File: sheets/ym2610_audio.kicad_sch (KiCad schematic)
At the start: 56 parts, among them J3 SMK S-G8043, Q101 2SC1815, Q102 2SC1815, U26 YM3016D, U27 YM2610, U28 PC4741, U29 PC4741

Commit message: Schematics Footprint updates
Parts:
- U26: footprint Package_DIP:DIP-16_W7.62mm -> 1_NeoGeoLibrary:DIP-16_W7.62mm
- U28, U29: footprint Package_DIP:DIP-14_W7.62mm -> 1_NeoGeoLibrary:DIP-14_W7.62mm
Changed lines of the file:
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@@
       (effects (font (size 1.27 1.27)))
     )
-    (property "Footprint" "Package_DIP:DIP-14_W7.62mm" (at 322.072 53.721 0)
+    (property "Footprint" "1_NeoGeoLibrary:DIP-14_W7.62mm" (at 322.072 53.721 0)
       (effects (font (size 1.27 1.27)) hide)
     )
@@
       (effects (font (size 1.27 1.27)))
     )
-    (property "Footprint" "Package_DIP:DIP-14_W7.62mm" (at 207.264 51.181 0)
+    (property "Footprint" "1_NeoGeoLibrary:DIP-14_W7.62mm" (at 207.264 51.181 0)
       (effects (font (size 1.27 1.27)) hide)
     )
@@
       (effects (font (size 1.27 1.27)))
     )
-    (property "Footprint" "Package_DIP:DIP-14_W7.62mm" (at 239.776 84.201 0)
+    (property "Footprint" "1_NeoGeoLibrary:DIP-14_W7.62mm" (at 239.776 84.201 0)
       (effects (font (size 1.27 1.27)) hide)
     )
@@
       (effects (font (size 1.27 1.27)))
     )
-    (property "Footprint" "Package_DIP:DIP-14_W7.62mm" (at 149.479 210.693 0)
+    (property "Footprint" "1_NeoGeoLibrary:DIP-14_W7.62mm" (at 149.479 210.693 0)
       (effects (font (size 1.27 1.27)) hide)
     )
@@
       (effects (font (size 1.27 1.27)))
     )
-    (property "Footprint" "Package_DIP:DIP-14_W7.62mm" (at 239.776 119.761 0)
+    (property "Footprint" "1_NeoGeoLibrary:DIP-14_W7.62mm" (at 239.776 119.761 0)
       (effects (font (size 1.27 1.27)) hide)
     )
@@
       (effects (font (size 1.27 1.27)))
     )
-    (property "Footprint" "Package_DIP:DIP-16_W7.62mm" (at 179.324 132.461 0)
+    (property "Footprint" "1_NeoGeoLibrary:DIP-16_W7.62mm" (at 179.324 132.461 0)
       (effects (font (size 1.27 1.27)) hide)
     )
@@
       (effects (font (size 1.27 1.27)))
     )
-    (property "Footprint" "Package_DIP:DIP-14_W7.62mm" (at 322.072 81.661 0)
+    (property "Footprint" "1_NeoGeoLibrary:DIP-14_W7.62mm" (at 322.072 81.661 0)
       (effects (font (size 1.27 1.27)) hide)
     )
@@
       (effects (font (size 1.27 1.27)))
     )
-    (property "Footprint" "Package_DIP:DIP-14_W7.62mm" (at 149.479 224.663 0)
+    (property "Footprint" "1_NeoGeoLibrary:DIP-14_W7.62mm" (at 149.479 224.663 0)
       (effects (font (size 1.27 1.27)) hide)
     )
@@
       (effects (font (size 1.27 1.27)))
     )
-    (property "Footprint" "Package_DIP:DIP-14_W7.62mm" (at 239.776 155.321 0)
-      (effects (font (size 1.27 1.27)) hide)
-    )
+    (property "Footprint" "1_NeoGeoLibrary:DIP-14_W7.62mm" (at 239.776 155.321 0)
+      (effects (font (size 1.27 1.27)) hide)
+    )

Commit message: Final update to Schematics Footprints Silkscreens
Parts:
- C13, C14: value 0.0022uF -> 272M
- C22, C23: value 10uF -> 1nF
- R39, R40, R41, R42: value 4.7KΩ -> 1KΩ
- RV1: value Headphone Slider -> Headphone Slider (0-1K)
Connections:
- net GND: no longer RV1.3
- no-connect marks 0 -> 1
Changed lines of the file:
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@@
   (junction (at 169.164 109.601) (diameter 0) (color 0 0 0 0)
   )
-  (junction (at 58.928 217.551) (diameter 0) (color 0 0 0 0)
-  )
   (junction (at 114.3 217.678) (diameter 0) (color 0 0 0 0)
   )
@@
   (junction (at 119.761 224.663) (diameter 0) (color 0 0 0 0)
   )
+  (no_connect (at 58.928 220.218))
   (bus_entry (at 140.97 53.721) (size -2.54 2.54)
     (stroke (width 0) (type default))
@@
     (stroke (width 0) (type default))
   )
-  (wire (pts (xy 58.928 217.551) (xy 58.928 220.218))
-    (stroke (width 0) (type default))
-  )
   (wire (pts (xy 225.425 208.788) (xy 225.425 213.233))
     (stroke (width 0) (type default))
@@
       (effects (font (size 1.27 1.27)))
     )
-    (property "Value" "0.0022uF" (at 200.152 147.574 90)
+    (property "Value" "272M" (at 200.152 147.574 90)
       (effects (font (size 1.27 1.27)))
     )
@@
       (effects (font (size 1.27 1.27)) (justify right))
     )
-    (property "Value" "Headphone Slider" (at 54.991 212.09 90)
+    (property "Value" "Headphone Slider (0-1K)" (at 54.991 212.09 90)
       (effects (font (size 1.27 1.27)) (justify right))
     )
@@
       (effects (font (size 1.27 1.27)))
     )
-    (property "Value" "4.7KΩ" (at 271.018 60.96 90)
+    (property "Value" "1KΩ" (at 271.018 60.96 90)
       (effects (font (size 1.27 1.27)))
     )
@@
       (effects (font (size 1.27 1.27)))
     )
-    (property "Value" "4.7KΩ" (at 271.018 79.502 90)
+    (property "Value" "1KΩ" (at 271.018 79.502 90)
       (effects (font (size 1.27 1.27)))
     )
@@
       (effects (font (size 1.27 1.27)))
     )
-    (property "Value" "4.7KΩ" (at 287.782 79.502 90)
+    (property "Value" "1KΩ" (at 287.782 79.502 90)
       (effects (font (size 1.27 1.27)))
     )
@@
       (effects (font (size 1.27 1.27)))
     )
-    (property "Value" "4.7KΩ" (at 287.782 60.96 90)
+    (property "Value" "1KΩ" (at 287.782 60.96 90)
       (effects (font (size 1.27 1.27)))
     )
@@
   (symbol (lib_id "Device:C_Small") (at 58.928 249.555 0) (unit 1)
     (in_bom yes) (on_board yes) (dnp no) (fields_autoplaced)
-    (property "Reference" "C22" (at 61.595 248.2912 0)
+    (property "Reference" "C22" (at 62.23 248.9263 0)
       (effects (font (size 1.27 1.27)) (justify left))
     )
-    (property "Value" "10uF" (at 61.595 250.8312 0)
+    (property "Value" "1nF" (at 62.23 251.4663 0)
       (effects (font (size 1.27 1.27)) (justify left))
     )
@@
       (effects (font (size 1.27 1.27)) (justify left))
     )
-    (property "Value" "0.0022uF" (at 224.282 117.221 0)
+    (property "Value" "272M" (at 224.282 117.221 0)
       (effects (font (size 1.27 1.27)) (justify left))
     )
@@
       (effects (font (size 1.27 1.27)))
     )
-    (property "Value" "10uF" (at 62.865 186.817 0)
+    (property "Value" "1nF" (at 62.865 186.817 0)
       (effects (font (size 1.27 1.27)))
     )

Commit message: Some tweaks
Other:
- company: (none) -> SNK
- title: (none) -> NeoGeo AES
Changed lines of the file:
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@@
 (kicad_sch (version 20230121) (generator eeschema)
   (paper "A3")
+  (title_block
+    (title "NeoGeo AES")
+    (date "2023-08-19")
+    (rev "3.5")
+    (company "SNK")
+    (comment 3 "https://github.com/Board-Folk")
+    (comment 4 "Recreated By The Board Folk Team")
+  )
   (junction (at 128.905 135.001) (diameter 0) (color 0 0 0 0)
   )

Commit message: Updates to PCB Move P2 Joystick Port Move Memory Card Move Holes at top right Silkscreen added Update Titles
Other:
- title: NeoGeo AES -> NeoGeo AES 3-5
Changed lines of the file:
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@@
   (paper "A3")
   (title_block
-    (title "NeoGeo AES")
-    (date "2023-08-19")
-    (rev "3.5")
+    (title "NeoGeo AES 3-5")
+    (date "2023-08-27")
+    (rev "BF1.1")
     (company "SNK")
     (comment 3 "https://github.com/Board-Folk")

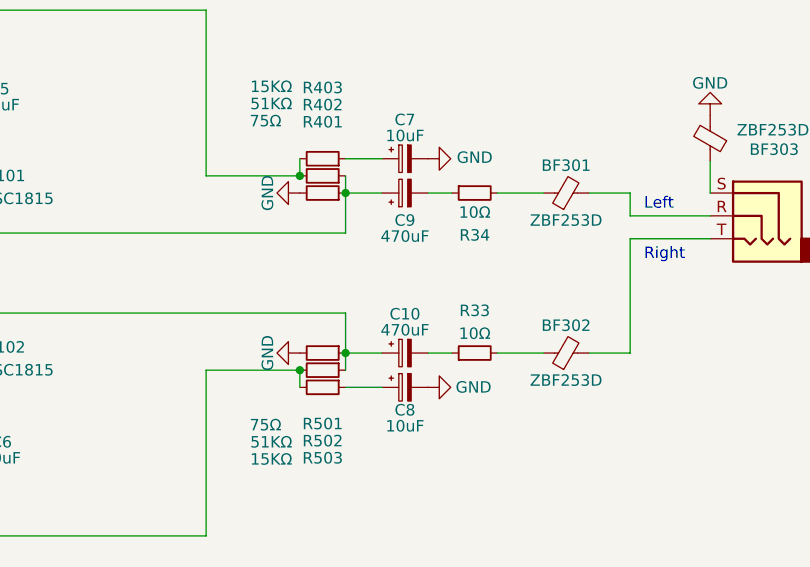
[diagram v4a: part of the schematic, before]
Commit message: Adding Mouser Part Numbers
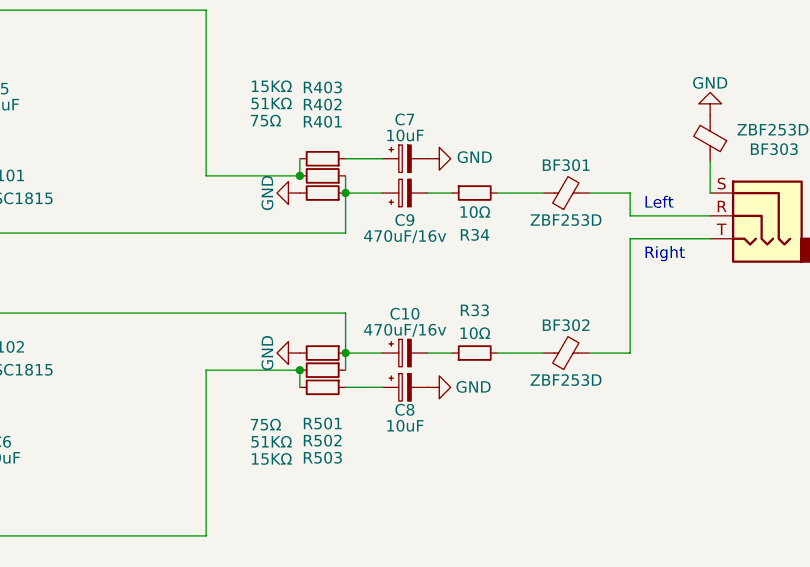
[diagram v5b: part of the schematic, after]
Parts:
- BF301, BF302, BF303: Mouser (none) -> 80-B-06-R-25
- C10, C9: value 470uF -> 470uF/16v; Mouser (none) -> 647-UHE1C471MPD6
- C11, C12, C2, C20, C24, C25, C301, C4, C5, C6, C7, C8: Mouser (none) -> 667-ECA-1CM100I
- C13, C14: Mouser (none) -> 80-MMK5272K63J01TA18
- C22, C23: Mouser (none) -> 810-FG28C0G1H102JNT6
- C3: Mouser (none) -> 810-FG28C0G2A680JNT6

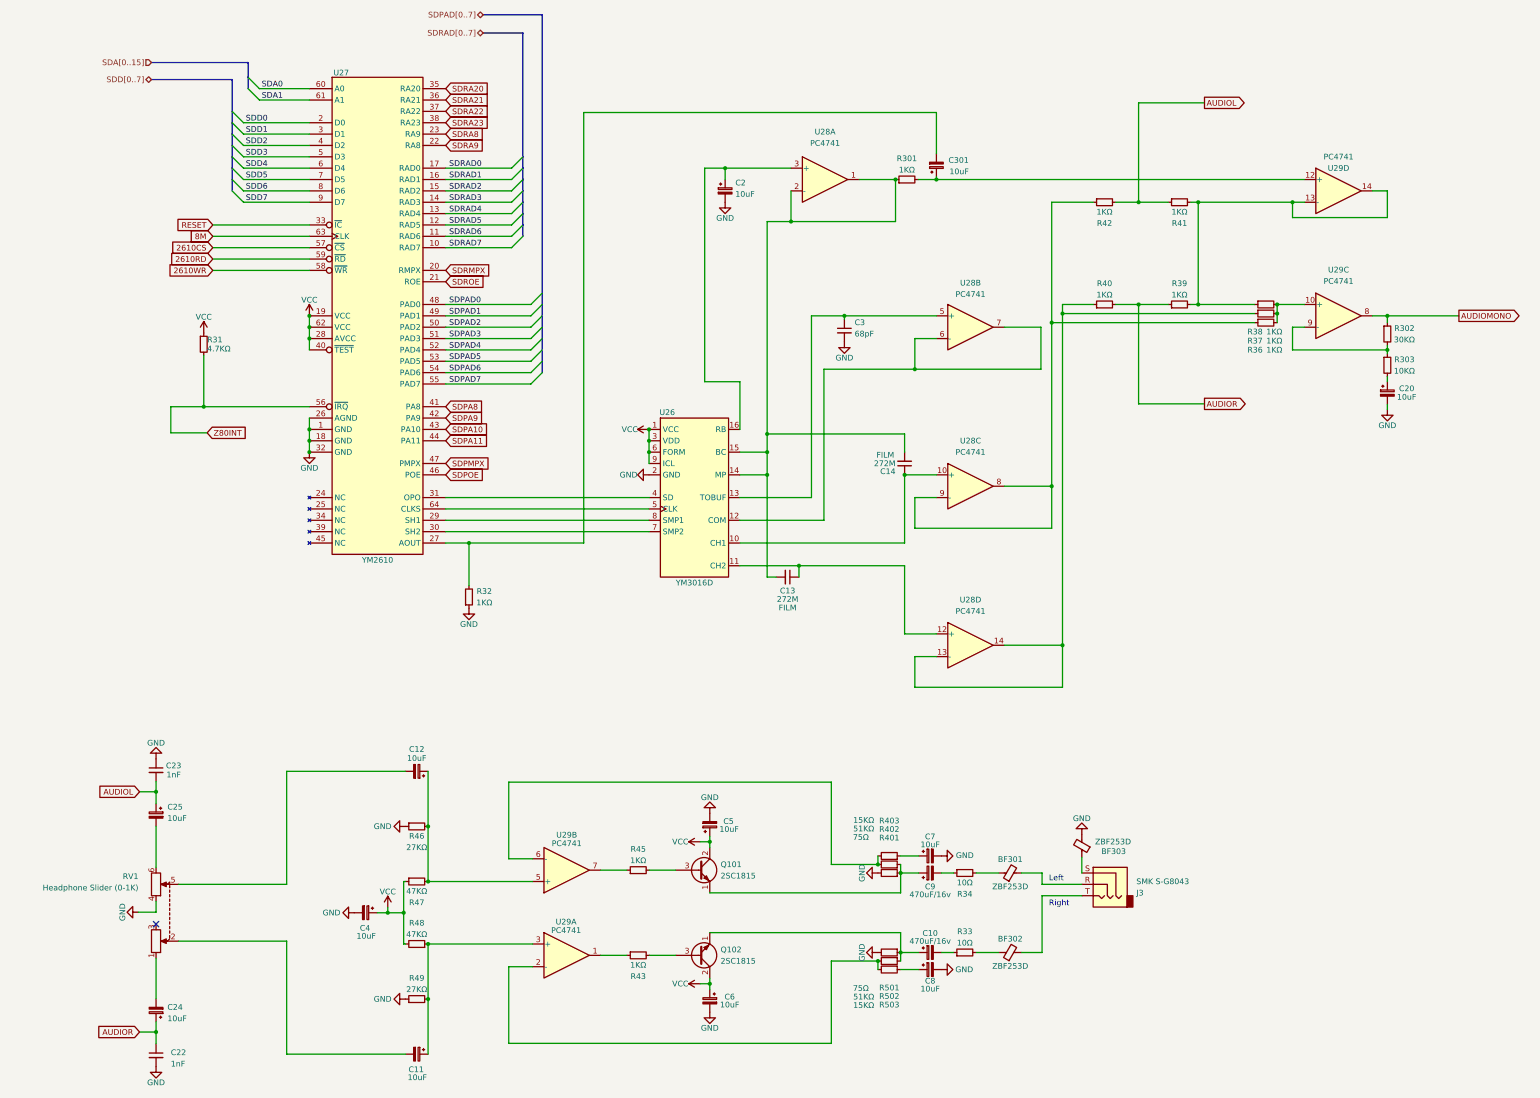
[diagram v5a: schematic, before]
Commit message: More silkscreen tidy up, adding mouser components to BOM
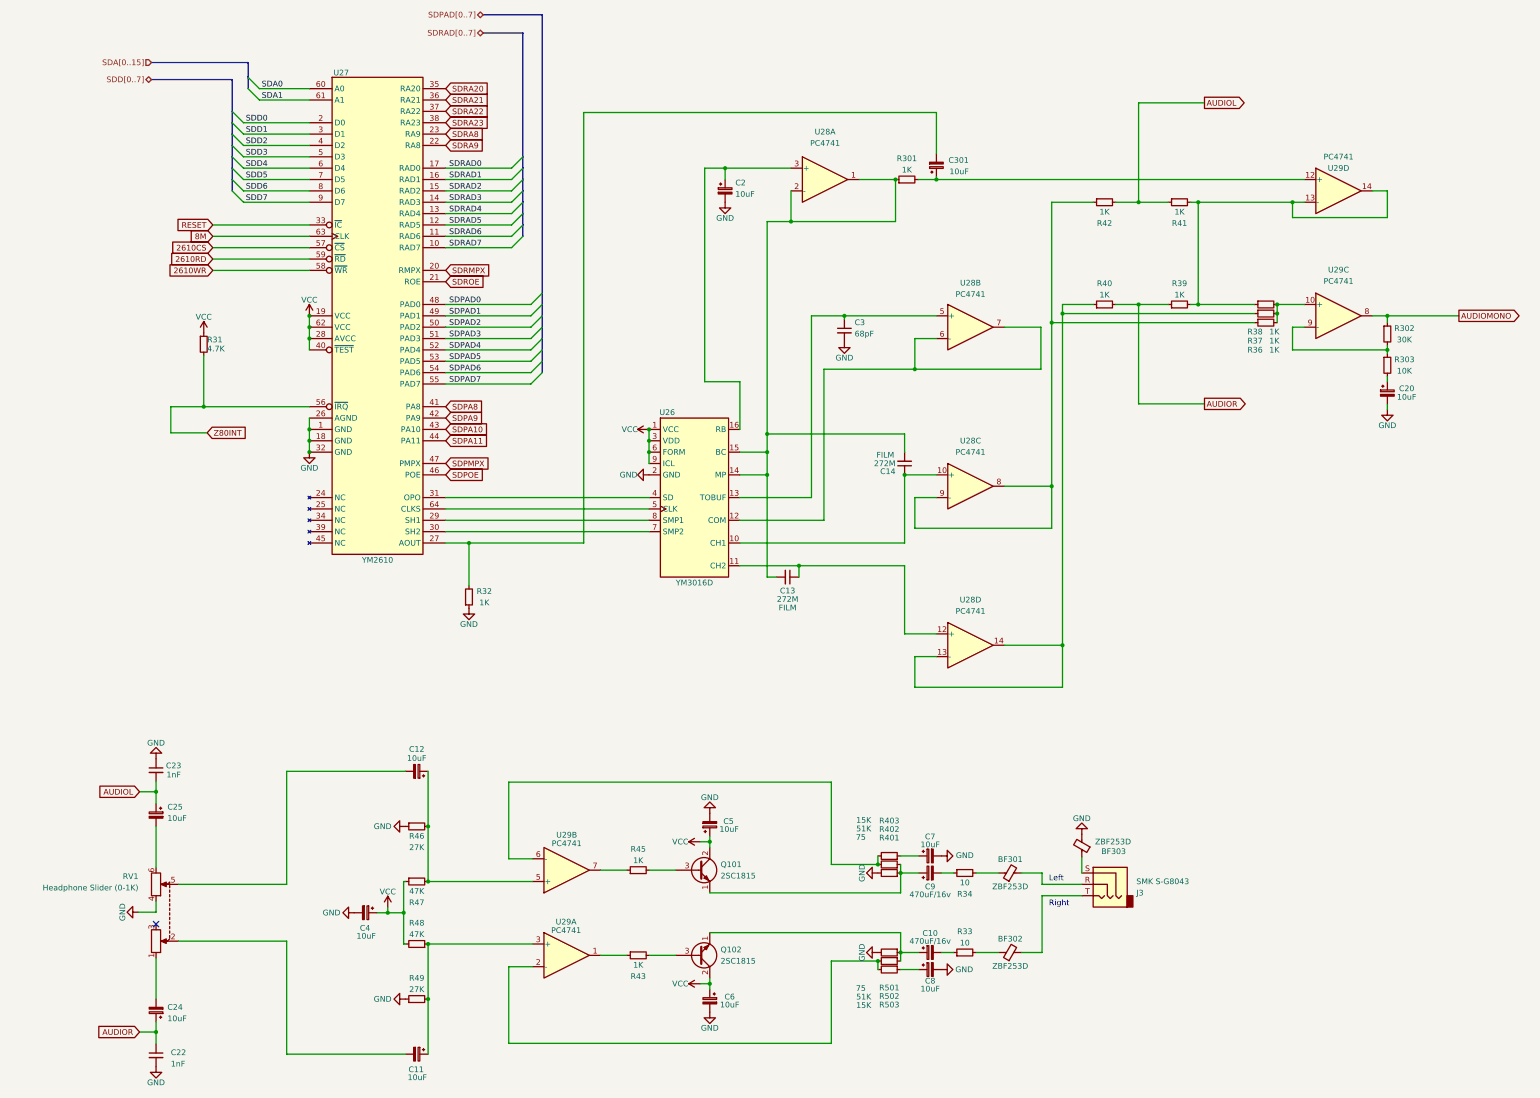
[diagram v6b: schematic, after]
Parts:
- Q101, Q102: Mouser (none) -> 610-2SC1815
- R301, R32, R36, R37, R38, R39, R40, R41, R42, R43, R45: value 1KΩ -> 1K
- R302: value 30KΩ -> 30K
- R303: value 10KΩ -> 10K
- R31: value 4.7KΩ -> 4.7K
- R33, R34: value 10Ω -> 10
- R401, R501: value 75Ω -> 75
- R402, R502: value 51KΩ -> 51K
- R403, R503: value 15KΩ -> 15K
- R46, R49: value 27KΩ -> 27K
- R47, R48: value 47KΩ -> 47K
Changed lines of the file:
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@@
       (effects (font (size 1.27 1.27)))
     )
-    (property "Value" "1KΩ" (at 166.751 205.994 90)
+    (property "Value" "1K" (at 166.751 205.994 90)
       (effects (font (size 1.27 1.27)))
     )
@@
       (effects (font (size 1.27 1.27)))
     )
-    (property "Value" "10KΩ" (at 338.074 96.52 0)
+    (property "Value" "10K" (at 338.074 96.52 0)
       (effects (font (size 1.27 1.27)))
     )
@@
       (effects (font (size 1.27 1.27)))
     )
-    (property "Value" "1KΩ" (at 166.751 229.362 90)
+    (property "Value" "1K" (at 166.751 229.362 90)
       (effects (font (size 1.27 1.27)))
     )
@@
       (effects (font (size 1.27 1.27)))
     )
-    (property "Value" "51KΩ" (at 217.17 198.882 90)
+    (property "Value" "51K" (at 217.17 198.882 90)
       (effects (font (size 1.27 1.27)))
     )
@@
       (effects (font (size 1.27 1.27)) (justify left) hide)
     )
-    (property "Mouser" "" (at 180.213 208.153 0)
+    (property "Mouser" "610-2SC1815" (at 180.213 208.153 0)
       (effects (font (size 1.27 1.27)) hide)
     )
@@
       (effects (font (size 1.27 1.27)))
     )
-    (property "Value" "1KΩ" (at 308.991 87.757 90)
+    (property "Value" "1K" (at 308.991 87.757 90)
       (effects (font (size 1.27 1.27)))
     )
@@
       (effects (font (size 1.27 1.27)))
     )
-    (property "Value" "15KΩ" (at 217.17 238.379 90)
+    (property "Value" "15K" (at 217.17 238.379 90)
       (effects (font (size 1.27 1.27)))
     )
@@
       (effects (font (size 1.27 1.27)) (justify left) hide)
     )
-    (property "Mouser" "" (at 180.213 227.203 0)
+    (property "Mouser" "610-2SC1815" (at 180.213 227.203 0)
       (effects (font (size 1.27 1.27)) hide)
     )
@@
       (effects (font (size 1.27 1.27)))
     )
-    (property "Value" "1KΩ" (at 308.991 89.789 90)
+    (property "Value" "1K" (at 308.991 89.789 90)
       (effects (font (size 1.27 1.27)))
     )
@@
       (effects (font (size 1.27 1.27)))
     )
-    (property "Value" "47KΩ" (at 117.221 212.852 90)
+    (property "Value" "47K" (at 117.221 212.852 90)
       (effects (font (size 1.27 1.27)))
     )
@@
       (effects (font (size 1.27 1.27)))
     )
-    (property "Value" "1KΩ" (at 271.018 60.96 90)
+    (property "Value" "1K" (at 271.018 60.96 90)
       (effects (font (size 1.27 1.27)))
     )
@@
       (effects (font (size 1.27 1.27)))
     )
-    (property "Value" "27KΩ" (at 117.221 203.073 90)
+    (property "Value" "27K" (at 117.221 203.073 90)
       (effects (font (size 1.27 1.27)))
     )
@@
       (effects (font (size 1.27 1.27)))
     )
-    (property "Value" "10Ω" (at 239.776 224.409 90)
+    (property "Value" "10" (at 239.776 224.409 90)
       (effects (font (size 1.27 1.27)))
     )
@@
       (effects (font (size 1.27 1.27)))
     )
-    (property "Value" "10Ω" (at 239.776 210.947 90)
+    (property "Value" "10" (at 239.776 210.947 90)
       (effects (font (size 1.27 1.27)))
     )
@@
       (effects (font (size 1.27 1.27)))
     )
-    (property "Value" "75Ω" (at 216.535 234.569 90)
+    (property "Value" "75" (at 216.535 234.569 90)
       (effects (font (size 1.27 1.27)))
     )
@@
       (effects (font (size 1.27 1.27)))
     )
-    (property "Value" "1KΩ" (at 271.018 79.502 90)
+    (property "Value" "1K" (at 271.018 79.502 90)
       (effects (font (size 1.27 1.27)))
     )
@@
       (effects (font (size 1.27 1.27)) (justify left))
     )
-    (property "Value" "4.7KΩ" (at 70.358 91.567 0)
+    (property "Value" "4.7K" (at 70.358 91.567 0)
       (effects (font (size 1.27 1.27)) (justify left))
     )
@@
       (effects (font (size 1.27 1.27)))
     )
-    (property "Value" "1KΩ" (at 287.782 79.502 90)
+    (property "Value" "1K" (at 287.782 79.502 90)
       (effects (font (size 1.27 1.27)))
     )
@@
       (effects (font (size 1.27 1.27)))
     )
-    (property "Value" "1KΩ" (at 287.782 60.96 90)
+    (property "Value" "1K" (at 287.782 60.96 90)
       (effects (font (size 1.27 1.27)))
     )
@@
       (effects (font (size 1.27 1.27)))
     )
-    (property "Value" "47KΩ" (at 117.221 222.504 90)
+    (property "Value" "47K" (at 117.221 222.504 90)
       (effects (font (size 1.27 1.27)))
     )
@@
       (effects (font (size 1.27 1.27)))
     )
-    (property "Value" "15KΩ" (at 217.17 196.977 90)
+    (property "Value" "15K" (at 217.17 196.977 90)
       (effects (font (size 1.27 1.27)))
     )
@@
       (effects (font (size 1.27 1.27)))
     )
-    (property "Value" "51KΩ" (at 217.17 236.474 90)
+    (property "Value" "51K" (at 217.17 236.474 90)
       (effects (font (size 1.27 1.27)))
     )
@@
       (effects (font (size 1.27 1.27)))
     )
-    (property "Value" "1KΩ" (at 308.991 91.821 90)
+    (property "Value" "1K" (at 308.991 91.821 90)
       (effects (font (size 1.27 1.27)))
     )
@@
       (effects (font (size 1.27 1.27)))
     )
-    (property "Value" "1KΩ" (at 132.334 148.336 0)
+    (property "Value" "1K" (at 132.334 148.336 0)
       (effects (font (size 1.27 1.27)))
     )
@@
       (effects (font (size 1.27 1.27)))
     )
-    (property "Value" "1KΩ" (at 226.822 51.562 90)
+    (property "Value" "1K" (at 226.822 51.562 90)
       (effects (font (size 1.27 1.27)))
     )
@@
       (effects (font (size 1.27 1.27)))
     )
-    (property "Value" "30KΩ" (at 338.074 89.535 0)
+    (property "Value" "30K" (at 338.074 89.535 0)
       (effects (font (size 1.27 1.27)))
     )
@@
       (effects (font (size 1.27 1.27)))
     )
-    (property "Value" "75Ω" (at 216.535 200.787 90)
+    (property "Value" "75" (at 216.535 200.787 90)
       (effects (font (size 1.27 1.27)))
     )
@@
       (effects (font (size 1.27 1.27)))
     )
-    (property "Value" "27KΩ" (at 117.221 234.823 90)
-      (effects (font (size 1.27 1.27)))
-    )
+    (property "Value" "27K" (at 117.221 234.823 90)
+      (effects (font (size 1.27 1.27)))
+    )

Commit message: Little tweaks to silkscreen Updated BOM with mouser parts
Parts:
- R301, R32, R36, R37, R38, R39, R40, R41, R42, R43, R45: Mouser (none) -> 71-CMF501K0000FHEA
- R302: Mouser (none) -> 71-RN60D-F-30K
- R303: Mouser (none) -> 71-RN60E1002F
- R31: Mouser (none) -> 71-RN60D4701F
- R33, R34: Mouser (none) -> 71-CMF5010R000FHEK
- R401, R501: Mouser (none) -> 71-CMF5075R000FHEB
- R402, R502: Mouser (none) -> 71-RN60D5102F
- R403, R503: Mouser (none) -> 71-CMF5015K000FHEK
- R46, R49: Mouser (none) -> 71-RN60D-F-27K
- R47, R48: Mouser (none) -> 71-RN60D4702F
- RV1, U26, U27, U28, U29: Comment (none) -> Use Original
